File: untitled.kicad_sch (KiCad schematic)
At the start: 34 parts, among them Q2 NMOS, Q3 NMOS, U4 TLV3501AID, U5 DGS0010A, U6 OPA2392, U7 ADC10065

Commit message: schematics done
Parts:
- removed R14, R15: R, symbol Device:R
- added C1: 100p, Capacitor_SMD:C_0603_1608Metric_Pad1.08x0.95mm_HandSolder, symbol Device:C
- added R3, R7: 1k, Resistor_SMD:R_0603_1608Metric_Pad0.98x0.95mm_HandSolder, symbol Device:R
- added R4: 12, Resistor_SMD:R_0603_1608Metric_Pad0.98x0.95mm_HandSolder, symbol Device:R
- R13, R21: value R -> 1k; footprint (none) -> Resistor_SMD:R_0603_1608Metric_Pad0.98x0.95mm_HandSolder
- R6: value R -> 12; footprint (none) -> Resistor_SMD:R_0603_1608Metric_Pad0.98x0.95mm_HandSolder
- U6: footprint (none) -> Package_SO:SOIC-8_3.9x4.9mm_P1.27mm
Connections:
- net AMPLIFIED_SIGNAL: now also R7.2; no longer R29.2, U4.3 (+)
- net EN_SIGNAL_D: now also R4.1
- net GND: now also C1.1
- net P3V3: now also C18.2, C19.2, U7.10 (VDDA), U7.2 (VDDA), U7.5 (IRS), U7.9 (VDDA)
- net SIGNAL_UNAMPLIFIED: now also R3.2
- net at Q3.2 (G): now also R3.1, R4.2
- net MOSI renamed DAC_MOSI
- net SCLK renamed DAC_SCLK
- new net: C1.2, R29.2, R7.1, U4.3 (+)
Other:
- note removed: "TODO: new schematic symbol for OPA 2392 (missing EN) find out if mosfet input of analog signal is ok"
- moved on the sheet: C10, C11, C12, C13, C18, C19, C20, C21, C22, C23, C24, C25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

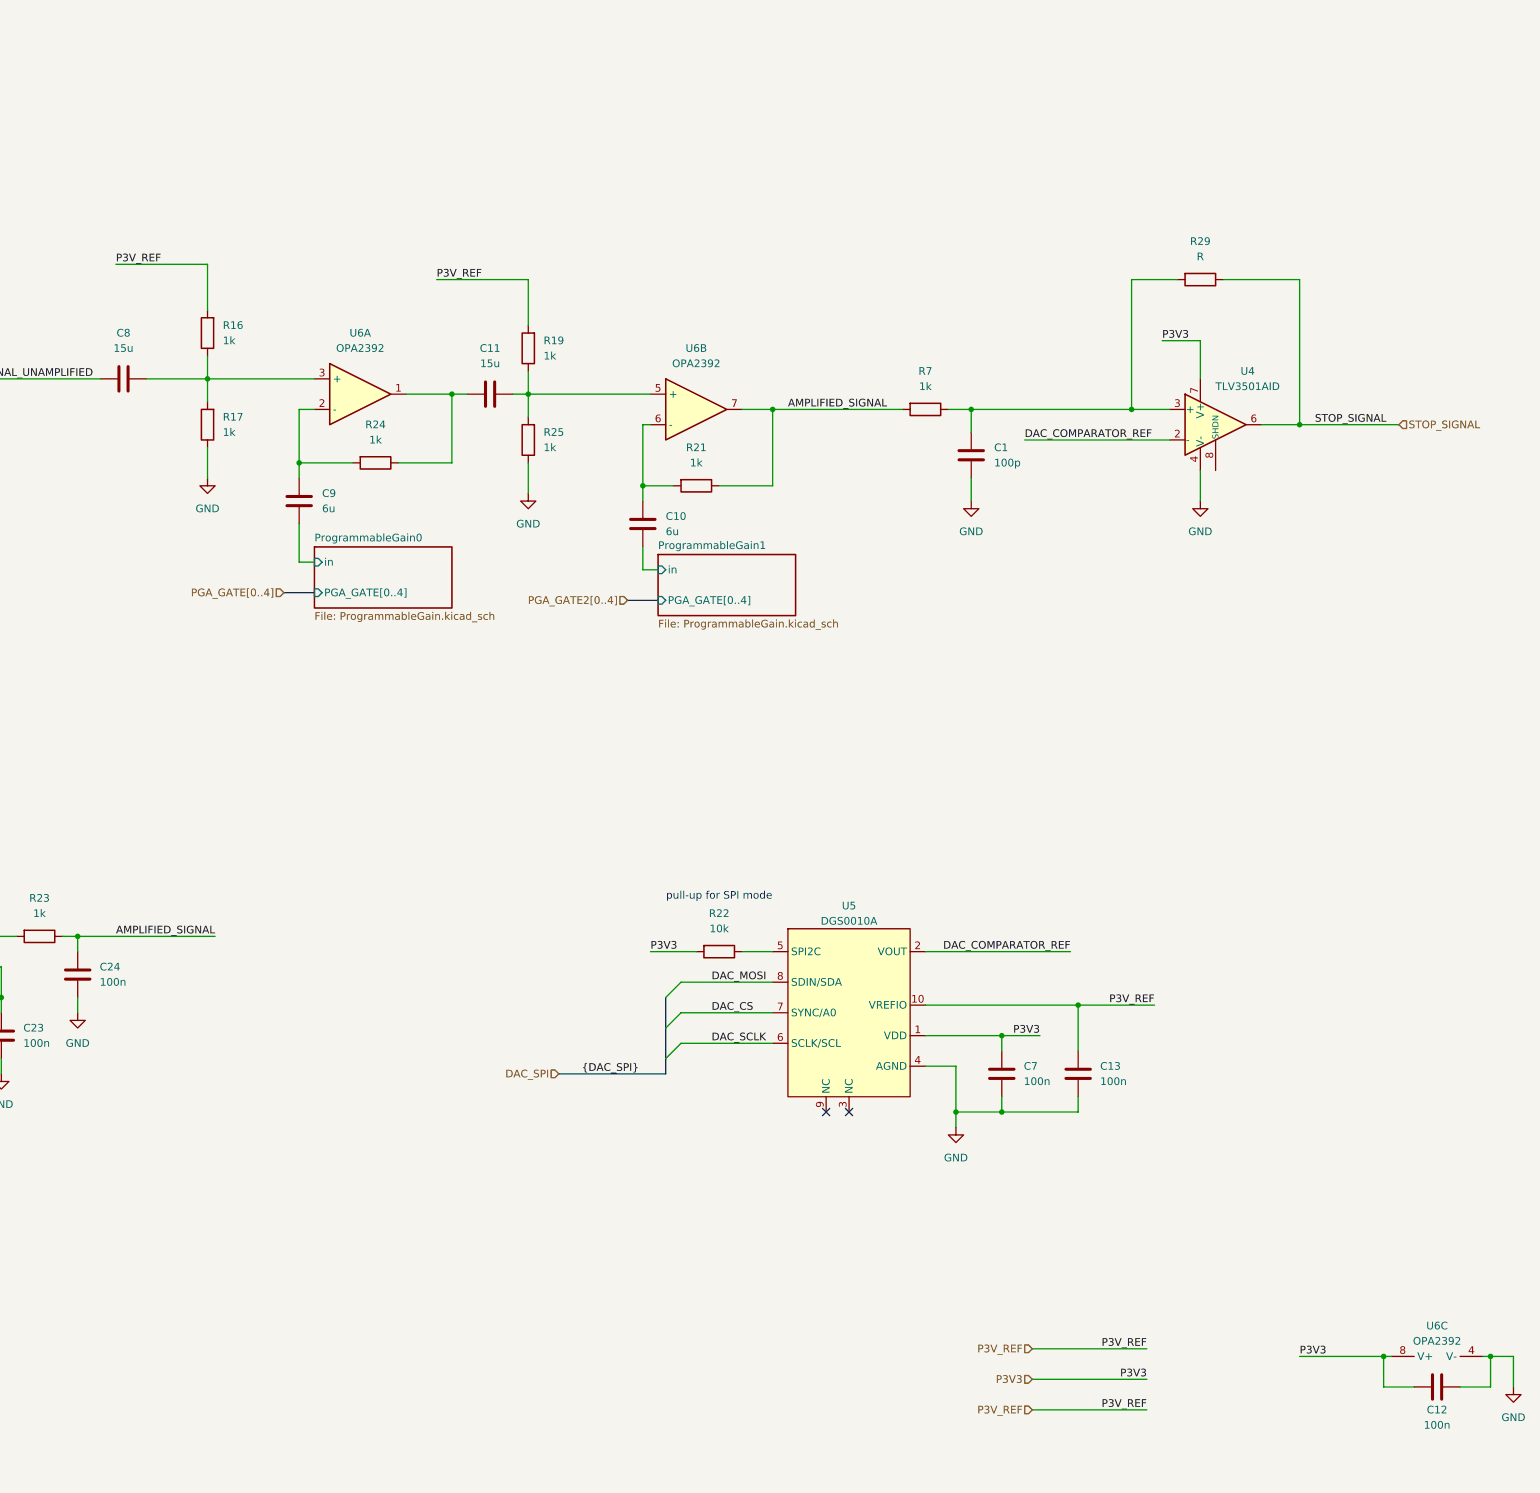
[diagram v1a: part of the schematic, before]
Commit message: ready schematic for layout
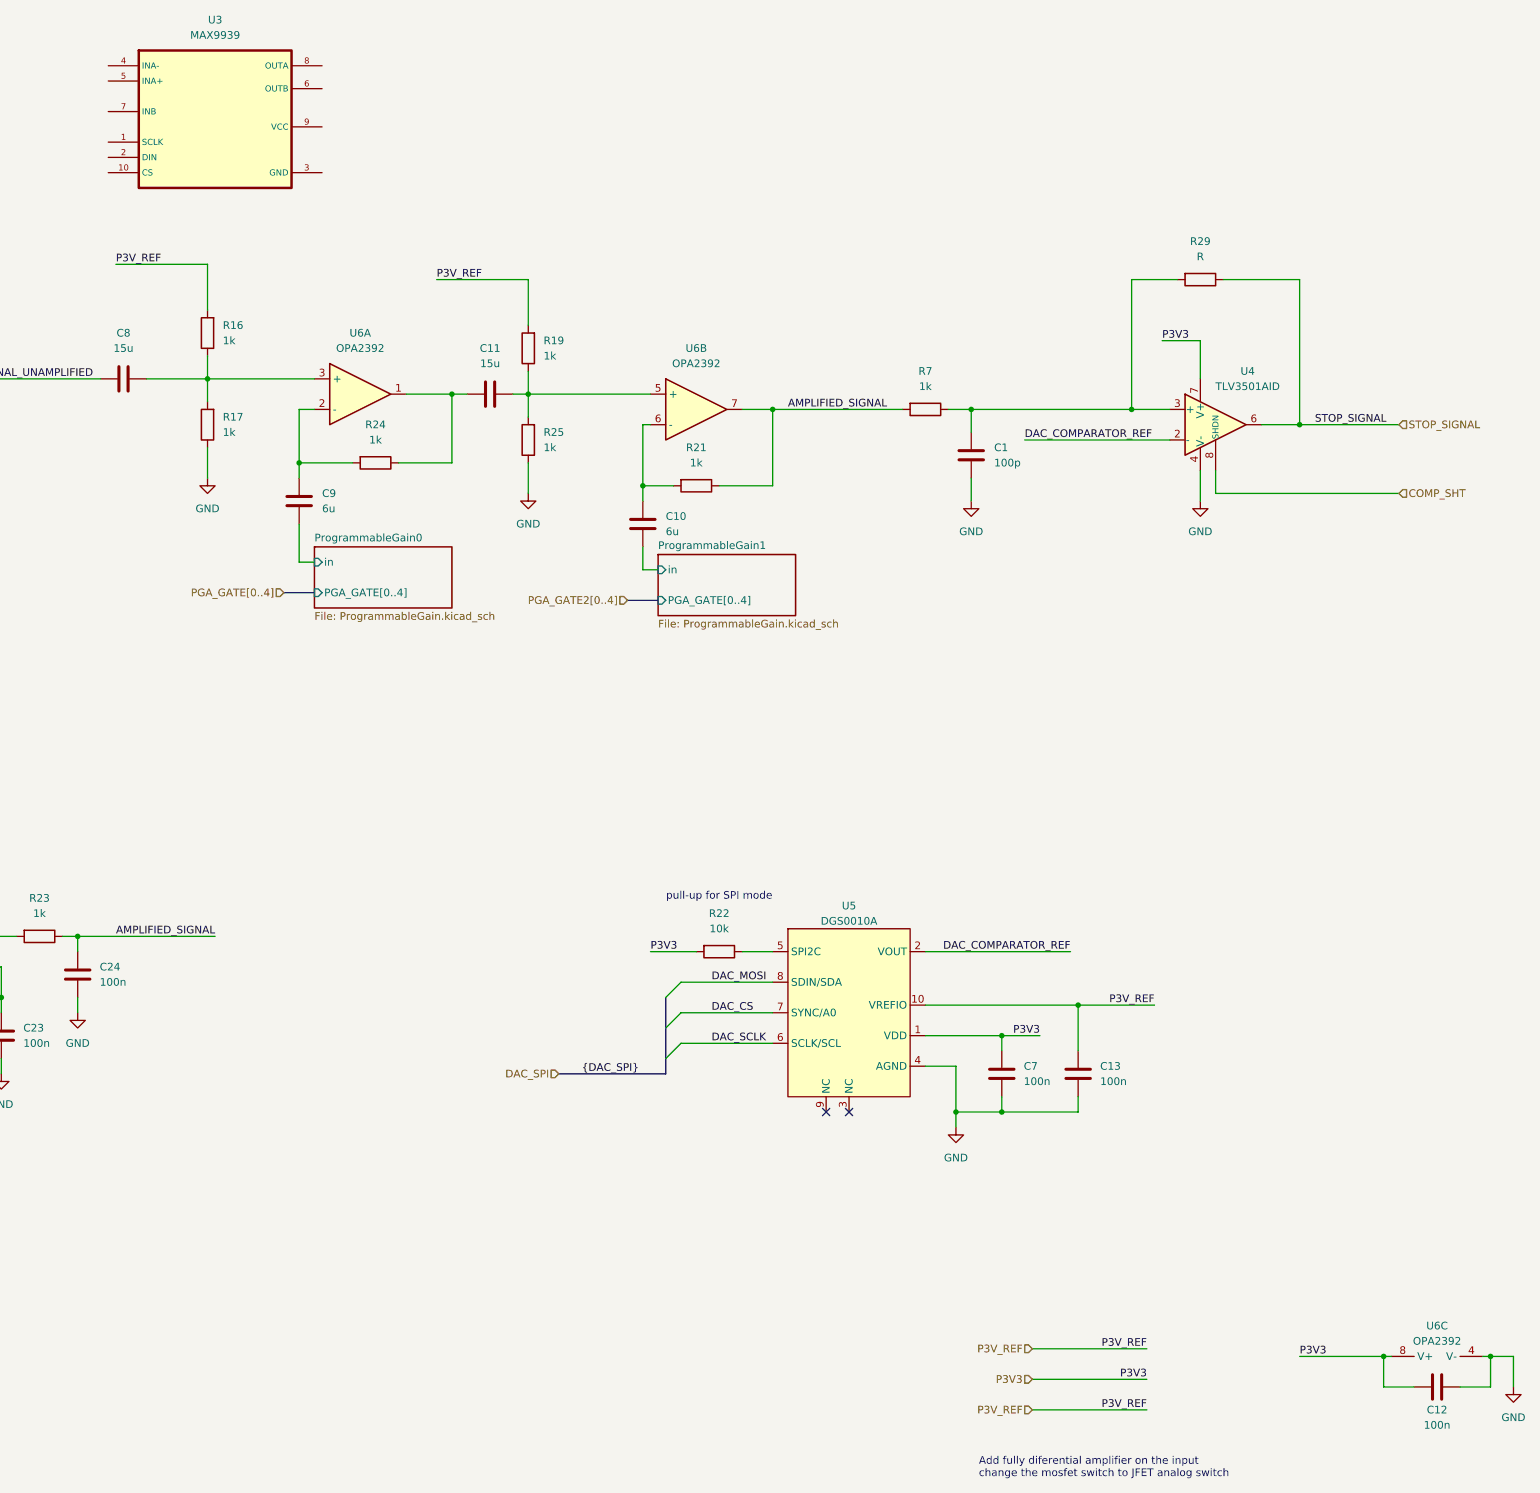
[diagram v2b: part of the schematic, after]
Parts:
- added U3: MAX9939, SpecialStuff:uMAX 10 pin, symbol 10_ICs:MAX9939
- R24, R29: footprint (none) -> Resistor_SMD:R_0603_1608Metric_Pad0.98x0.95mm_HandSolder
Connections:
- net COMP_SHT: now reaches U4.8 (SHDN)
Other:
- note added: "Add fully diferential amplifier on the input change the mosfet switch to JFET analog switch"
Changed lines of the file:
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@@
 		)
 	)
+	(wire
+		(pts
+			(xy 370.84 93.98) (xy 340.36 93.98)
+		)
+		(stroke
+			(width 0)
+			(type default)
+		)
+	)
 	(bus
 		(pts
@@
 	(wire
 		(pts
+			(xy 340.36 93.98) (xy 340.36 90.17)
+		)
+		(stroke
+			(width 0)
+			(type default)
+		)
+	)
+	(wire
+		(pts
 			(xy 123.19 231.14) (xy 110.49 231.14)
 		)
@@
 		)
 	)
+	(text "Add fully diferential amplifier on the input \nchange the mosfet switch to JFET analog switch"
+		(exclude_from_sim no)
+		(at 300.99 256.032 0)
+		(effects
+			(font
+				(size 1.27 1.27)
+			)
+			(justify left)
+		)
+	)
 	(label "STOP_SIGNAL"
 		(at 356.87 82.55 0)
@@
 		)
 	)
+	(hierarchical_label "COMP_SHT"
+		(shape input)
+		(at 370.84 93.98 0)
+		(fields_autoplaced yes)
+		(effects
+			(font
+				(size 1.27 1.27)
+			)
+			(justify left)
+		)
+	)
 	(hierarchical_label "DAC_SPI"
 		(shape input)
@@
 	)
 	(symbol
+		(lib_id "10_ICs:MAX9939")
+		(at 161.29 20.32 0)
+		(unit 1)
+		(exclude_from_sim no)
+		(in_bom yes)
+		(on_board yes)
+		(dnp no)
+		(fields_autoplaced yes)
+		(property "Reference" "U3"
+			(at 173.99 15.24 0)
+			(effects
+				(font
+					(size 1.27 1.27)
+				)
+			)
+		)
+		(property "Value" "MAX9939"
+			(at 173.99 17.78 0)
+			(effects
+				(font
+					(size 1.27 1.27)
+				)
+			)
+		)
+		(property "Footprint" "SpecialStuff:uMAX 10 pin"
+			(at 161.29 20.32 0)
+			(effects
+				(font
+					(size 1.27 1.27)
+				)
+				(hide yes)
+			)
+		)
+		(property "Datasheet" ""
+			(at 161.29 20.32 0)
+			(effects
+				(font
+					(size 1.27 1.27)
+				)
+				(hide yes)
+			)
+		)
+		(property "Description" ""
+			(at 161.29 20.32 0)
+			(effects
+				(font
+					(size 1.27 1.27)
+				)
+				(hide yes)
+			)
+		)
+		(pin "8"
+		)
+		(pin "7"
+		)
+		(pin "1"
+		)
+		(pin "4"
+		)
+		(pin "10"
+		)
+		(pin "5"
+		)
+		(pin "3"
+		)
+		(pin "2"
+		)
+		(pin "9"
+		)
+		(pin "6"
+		)
+		(instances
+			(project "ultrasonic_V3_HW"
+				(path "/731d4032-cf8d-4f76-95ca-2ec44c8e0816/bbbd27e3-755b-468e-8e26-bb40916e3b9a"
+					(reference "U3")
+					(unit 1)
+				)
+			)
+		)
+	)
+	(symbol
 		(lib_id "power:GND")
 		(at 130.81 187.96 0)
@@
 			)
 		)
-		(property "Footprint" ""
+		(property "Footprint" "Resistor_SMD:R_0603_1608Metric_Pad0.98x0.95mm_HandSolder"
 			(at 337.82 56.642 90)
 			(effects
@@
 			)
 		)
-		(property "Footprint" ""
+		(property "Footprint" "Resistor_SMD:R_0603_1608Metric_Pad0.98x0.95mm_HandSolder"
 			(at 200.66 87.122 90)
 			(effects

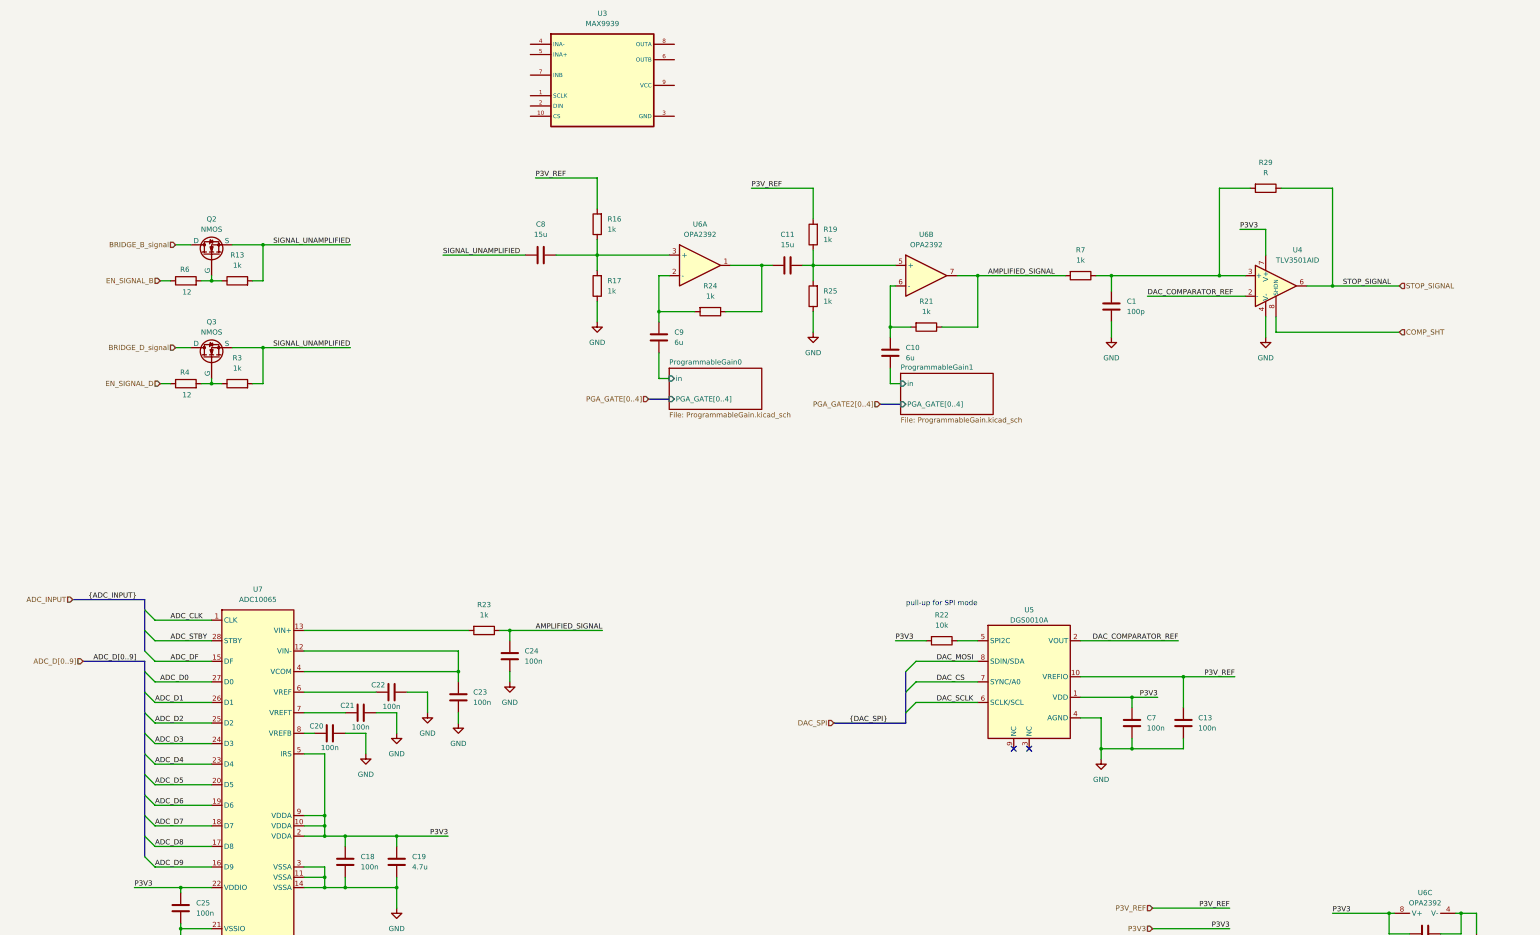
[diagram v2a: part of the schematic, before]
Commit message: new analog front end
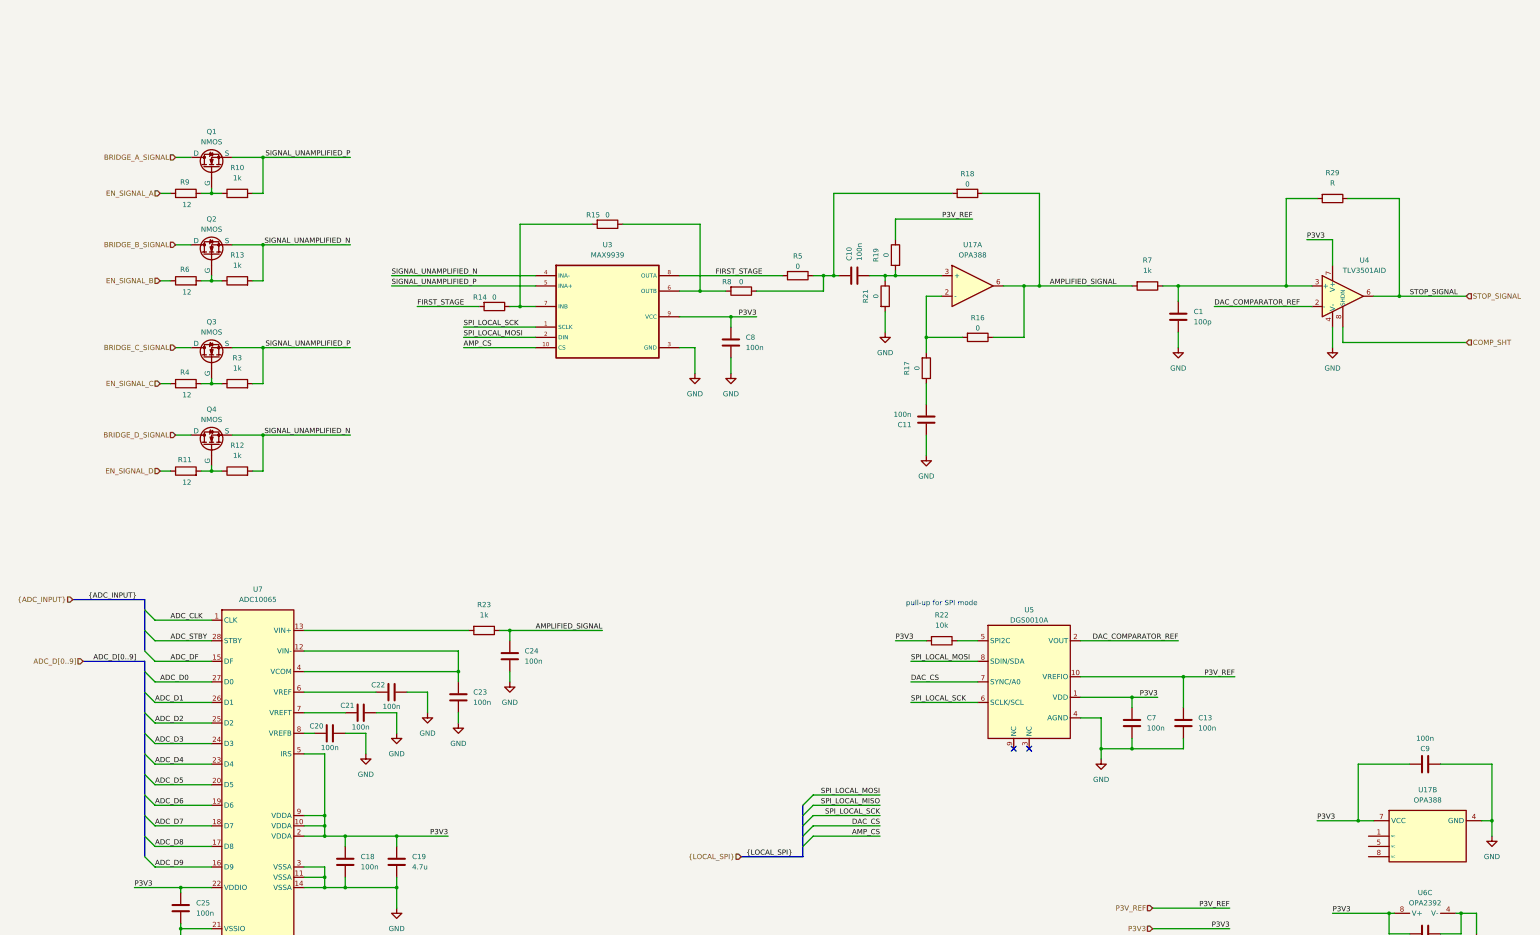
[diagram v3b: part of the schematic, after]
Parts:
- removed R24, R25: 1k, Resistor_SMD:R_0603_1608Metric_Pad0.98x0.95mm_HandSolder, symbol Device:R
- removed unit 1 of U6
- removed unit 2 of U6
- added Q1, Q4: NMOS, Package_TO_SOT_SMD:SOT-23_Handsoldering, symbol Simulation_SPICE:NMOS
- added R10, R12: 1k, Resistor_SMD:R_0603_1608Metric_Pad0.98x0.95mm_HandSolder, symbol Device:R
- added R11, R9: 12, Resistor_SMD:R_0603_1608Metric_Pad0.98x0.95mm_HandSolder, symbol Device:R
- added R14, R15, R18, R5, R8: 0, Resistor_SMD:R_0603_1608Metric_Pad0.98x0.95mm_HandSolder, symbol Device:R
- added U17: OPA388, Package_SO:VSSOP-8_3.0x3.0mm_P0.65mm, symbol 10_ICs:OPA388
- C10, C9: value 6u -> 100n; footprint Capacitor_SMD:C_0805_2012Metric_Pad1.18x1.45mm_HandSolder -> Capacitor_SMD:C_0603_1608Metric_Pad1.08x0.95mm_HandSolder
- C11, C8: value 15u -> 100n; footprint Capacitor_SMD:C_0805_2012Metric_Pad1.18x1.45mm_HandSolder -> Capacitor_SMD:C_0603_1608Metric_Pad1.08x0.95mm_HandSolder
- R16, R17, R19, R21: value 1k -> 0
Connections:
- net DAC_MOSI is gone; now on net SPI_LOCAL_MOSI: U5.8 (SDIN/SDA)
- net DAC_SCLK is gone; now on net SPI_LOCAL_SCK: U5.6 (SCLK/SCL)
- net ProgrammableGain0/in is gone; now on net P3V3: C9.1
- net AMPLIFIED_SIGNAL: now also R16.1, R18.1, U17.6; no longer R21.1
- net EN_SIGNAL_D: now also R11.1; no longer R4.1
- net GND: now also C11.2, C8.1, C9.2, R21.2, U3.3 (GND), U17.4 (GND); no longer R17.1
- net P3V3: now also C8.2, U3.9 (VCC), U17.7 (VCC)
- net P3V_REF: now also R19.1; no longer R16.2, R19.2
- net SPI_LOCAL_SCK: now reaches U3.1 (SCLK)
- net AMP_CS: now reaches U3.10 (CS)
- net SPI_LOCAL_MOSI: now reaches U3.2 (DIN)
- net SIGNAL_UNAMPLIFIED_N: now reaches U3.4 (INA-)
- net SIGNAL_UNAMPLIFIED_N: now also Q2.3 (S), R13.2, Q4.3 (S), R12.2
- net SIGNAL_UNAMPLIFIED_P: now reaches U3.5 (INA+)
- net SIGNAL_UNAMPLIFIED_P: now also Q3.3 (S), R3.2, Q1.3 (S), R10.2
- net at U3.6 (OUTB): now also R15.1, R8.2
- net at U3.7 (INB): now also R14.1, R15.2
- net FIRST_STAGE: now reaches U3.8 (OUTA)
- net FIRST_STAGE: now also R14.2, R5.2
- net at C11.1: now also R17.1
- net at C10.2: now also R18.2, R5.1, R8.1; no longer R21.2
- net BRIDGE_B_signal renamed BRIDGE_B_SIGNAL
- net BRIDGE_D_signal renamed BRIDGE_C_SIGNAL
- net ProgrammableGain1/in: no longer names the net of C10.1
- net ProgrammableGain1/in: now also R19.2, R21.1, U17.3 (+)
- removed net SIGNAL_UNAMPLIFIED: C8.1, Q2.3 (S), Q3.3 (S), R13.2, R3.2
- new net: R16.2, R17.2, U17.2 (-)
- new net: Q4.2 (G), R11.2, R12.1
- new net: Q1.2 (G), R10.1, R9.2
- new net BRIDGE_A_SIGNAL: Q1.1 (D)
- new net BRIDGE_D_SIGNAL: Q4.1 (D)
- new net EN_SIGNAL_A: R9.1
- new net EN_SIGNAL_C: R4.1
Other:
- removed sheet ProgrammableGain0
- removed sheet ProgrammableGain1
- moved on the sheet: C1, R29, R7, U3, U4
